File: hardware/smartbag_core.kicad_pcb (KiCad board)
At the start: 4 copper layers, 196 x 20 mm, 111 parts, among them J1 FFC optics, 12 way, J2 Jauch LP523450JU 950mAh, J3 Qi RX coil, J4 FFC FSR matrix, 24 way, J5 SWD debug, Q1 SI2302CDS-T1-GE3, U1 nRF54L15-QFAA-R, U11 BQ51013BRHLR, U2 Acconeer A121, U3 nPM1300-QEAA-R7, U4 BMI270, U5 DRV5032FBDBZR, U6 Acconeer A121, U7 CD74HC4067SM96, U8 TLV9064IPWR, U9 TLV9064IPWR, Y1 32 MHz Cl=8pF, Y2 24 MHz, Y3 24 MHz, Y4 32.768 kHz Cl=9pF

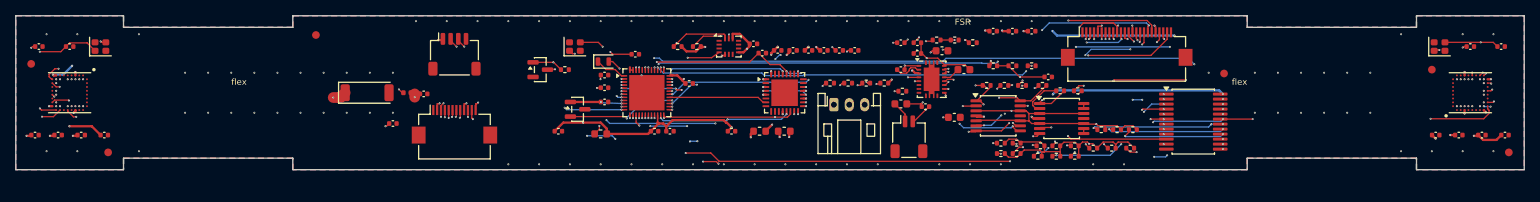
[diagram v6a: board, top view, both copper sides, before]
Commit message: The back side made it worse, twice, and the second time explained the first
U1's four decoupling capacitors were moved underneath it — the textbook answer
for a fine-pitch QFN on a dense board, and the one I recommended. It cost the
whole SPI bus.

Moving them to the back did not free the surface. It moved the congestion to
B.Cu, which is where the escapes land. The point of a fanout is that a signal
leaves the package on the top layer for 0.35 mm and then DROPS; on four layers
where In1 is an RF reference plane nobody routes on, the only routing layers
are F.Cu, In2 and B.Cu, and a QFN48 with thirty-five signals needs all three
under the package. Four capacitors on B.Cu under U1 sit exactly where those
signals arrive.

  old board, capacitors 3-6 mm from their pins      1 unconnected
  front, with the escape band kept clear            3
  back, with a via in each pad                      9
  back, with the router placing the vias           10  <- the whole SPI bus

So BACK is empty and the four numbers are in netlist.py, because that is where
somebody will next be tempted. Sub-millimetre decoupling AND a clear escape on
this part wants six layers: a second ground plane frees In2 for signals. That
is a cost decision and it is now written where it gets taken.

Two more of mine, on the same theme of deciding a geometry somewhere that
cannot see what is around it:

  - I moved five resistors 1.5 mm to win 0.14 mm on C43 and took the board from
    three unconnected to nine. The rule was wrong, not the floorplan: a 100 nF
    at a supply pin and a 1 uF reservoir on a cell input are doing different
    jobs and 2 mm is the answer to only one of them. check.py asks each the
    right question now — 2 mm for decoupling, 4 mm for bulk.
  - both hand repairs were coordinates read off the board, and both landed on
    copper they had not looked at: the pin-22 drop crossed I2C_SCL on In2, the
    FSR_R2 via came out 0.0012 mm from ADC4. A through via is an obstacle on
    four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
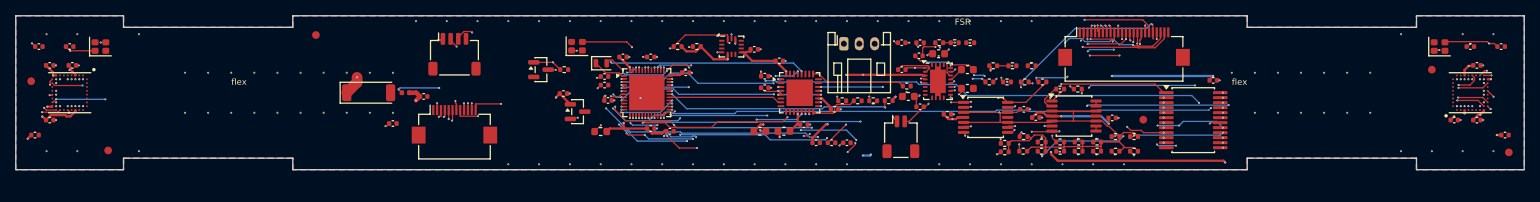
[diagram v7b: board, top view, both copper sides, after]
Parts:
- added C64: 100n X7R, Capacitor_SMD:C_0402_1005Metric, F.Cu at (267.6, 146.4)
- added C9: 100n X7R, Capacitor_SMD:C_0402_1005Metric, F.Cu at (190.9, 143.3)
- moved C63 15.4 mm to (254.5, 151.3)
- moved C61 12.3 mm to (233.1, 150.8)
- moved FID4 12.1 mm to (258.5, 151.5)
- moved C44 12.0 mm to (216.0, 154.5)
- moved C45 12.0 mm to (218.0, 154.5)
- moved C46 12.0 mm to (220.0, 154.5)
- moved C62 11.6 mm to (244.5, 151.2)
- moved C23 11.5 mm to (116.4, 144.4)
- moved C51 9.45 mm to (214.4, 152.1)
- moved C22 9.12 mm to (119.3, 144.4)
- moved C31 9.07 mm to (301.9, 144.4)
- moved C43 8.37 mm to (218.4, 150.2)
- moved J2 8.02 mm to (219.6, 141.6)
- moved C33 5.69 mm to (301.9, 151.6)
- moved C60 5.26 mm to (243.0, 150.2)
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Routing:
- net VDD_3V3: track 340.1 -> 309.5 mm, vias 29 -> 22
- net VSYS: track 69.6 -> 87.3 mm, vias 7 -> 6
- net VDD_CAM: track 60.9 -> 76.1 mm
- net I2C_SDA: track 68.3 -> 82.0 mm, vias 5 -> 6
- net ADC4: track 60.7 -> 72.8 mm
- net FSR_C12: track 48.1 -> 36.6 mm
- net QI_CLAMP1: track 14.2 -> 4.73 mm
- net RADAR_IRQ_R: track 120.3 -> 111.4 mm, vias 4 -> 3
- net TOF_XSHUT: track 30.6 -> 39.2 mm
- net FSR_R1: track 33.0 -> 41.4 mm, vias 4 -> 5
- net VDD_1V8: track 250.5 -> 242.2 mm, vias 21 -> 20
- net FSR_R4: track 32.1 -> 24.8 mm, vias 2 -> 3
- net SPI_MOSI: track 209.0 -> 216.0 mm, vias 6 -> 10
- net VBAT: track 18.1 -> 11.2 mm, vias 2 -> 1
- net DECRF: track 14.4 -> 7.77 mm
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
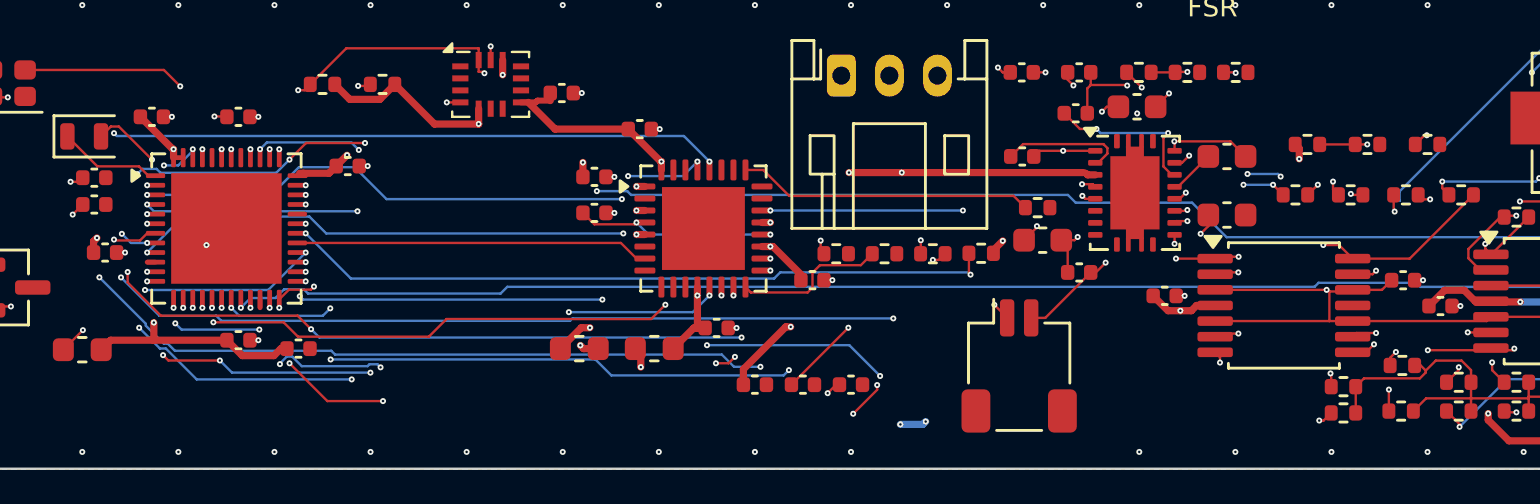
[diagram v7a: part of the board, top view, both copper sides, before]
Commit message: The tidy-up was removing the escapes, and that was the whole story
Both connections this board could not close were the same thing, and it was
self-inflicted. `maze.py --tidy` removes fanout vias that look unused — and a
via 0.35 mm outside a pad is not unused, it is the only thing standing between
that pad and the other three copper layers. Removing two of them stranded U1's
pins 10 and 22 on F.Cu inside a 0.4 mm escape row, and every router here then
reported, correctly, that there was no way out.

The islands said it plainly once I asked: a pad plus one stub track, ZERO vias,
against a main island of 150 tracks and 22 vias. Not a routing problem. A hole
somebody had filled in.

drop_dangling now spares any via whose island holds a pad and no other via, and
says how many it kept. FSR_R2 turned out to be the same family — a B.Cu track
finishing exactly on an F.Cu pad, zero-length ratsnest, no via — and closes with
one drop at (242.631, 147.295).

  3 unconnected -> 2, still 0 clearance violations and 0 shorts

Getting here cost four wrong acceptance tests, each of which deserves writing
down because each one looked right:

  - "fewer unconnected pads on the board" — KiCad reports one ratsnest line per
    NET, so closing one of a net's two breaks changes nothing and a correct
    repair is thrown away;
  - "the pair DRC named is gone" — KiCad picks a different representative item
    every run, so that is always true, and under it this file accepted twelve
    vias that connected nothing and called each a success;
  - counting islands with GetConnectedItems — reported two pieces where DRC
    plainly saw three;
  - "fewer breaks in THIS net", which is the one that works, because it is the
    same question put to the same referee that decides whether the board ships.

And three geometry mistakes of mine, all the same shape as the hardware ones:
proximity is not membership (candidate vias picked by distance landed on the
island I was trying to REACH, connecting noth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
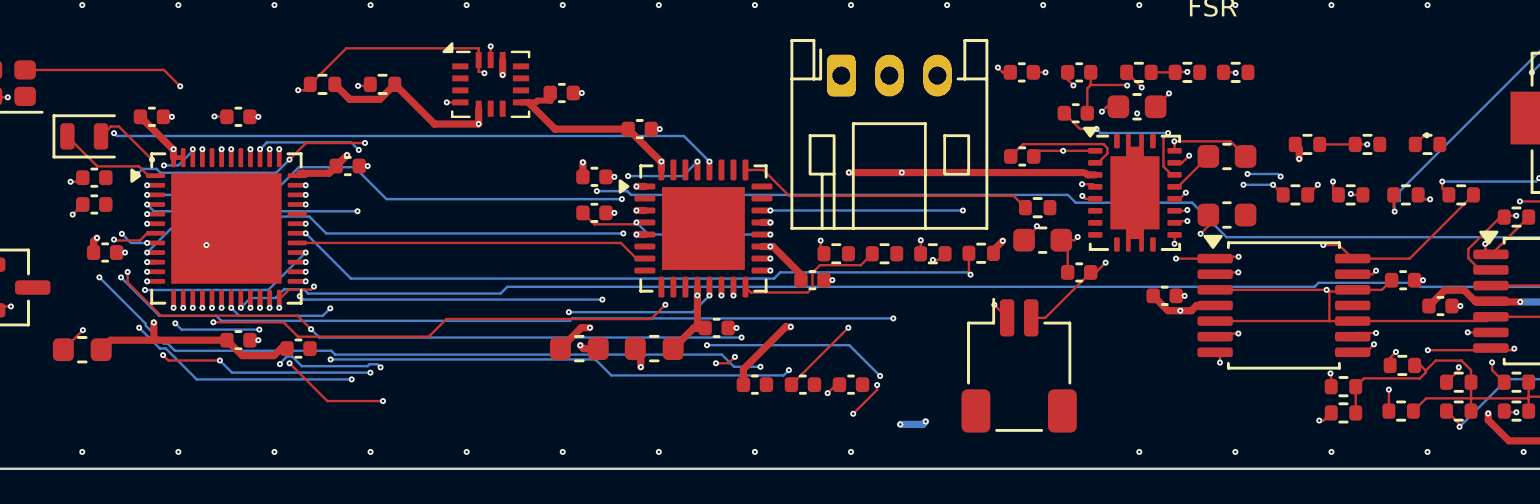
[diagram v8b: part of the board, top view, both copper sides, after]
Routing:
- net FSR_R2: track 34.8 -> 35.5 mm
- net VDD_3V3: vias 22 -> 24
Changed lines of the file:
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@@
 	)
 	(via
+		(at 190.7 149.4)
+		(size 0.25)
+		(drill 0.1)
+		(layers "F.Cu" "B.Cu")
+		(net "VDD_3V3")
+	)
+	(via
 		(at 226.3165 148.5148)
 		(size 0.25)
@@
 	)
 	(via
+		(at 195.4 151.3)
+		(size 0.25)
+		(drill 0.1)
+		(layers "F.Cu" "B.Cu")
+		(net "VDD_3V3")
+	)
+	(via
 		(at 247.861 151.0566)
 		(size 0.25)
@@
 	(segment
 		(start 191.8251 150.3192)
+		(end 191.8251 150.3192)
+		(width 0.3)
+		(layer "In2.Cu")
+		(net "VDD_3V3")
+	)
+	(segment
+		(start 191.8251 150.3192)
 		(end 190.9784 151.1659)
 		(width 0.3)
@@
 		(width 0.1)
 		(layer "B.Cu")
+		(net "FSR_R2")
+	)
+	(segment
+		(start 242.6309 147.2947)
+		(end 242.59 146.6)
+		(width 0.1)
+		(layer "B.Cu")
